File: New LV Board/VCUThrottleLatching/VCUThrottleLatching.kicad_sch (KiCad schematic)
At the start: 9 parts, among them J1 B12B-PH-K-S:JST_B12B-PH-K-S, U1 IRLML2060TRPBF, U2 IRLML2060TRPBF

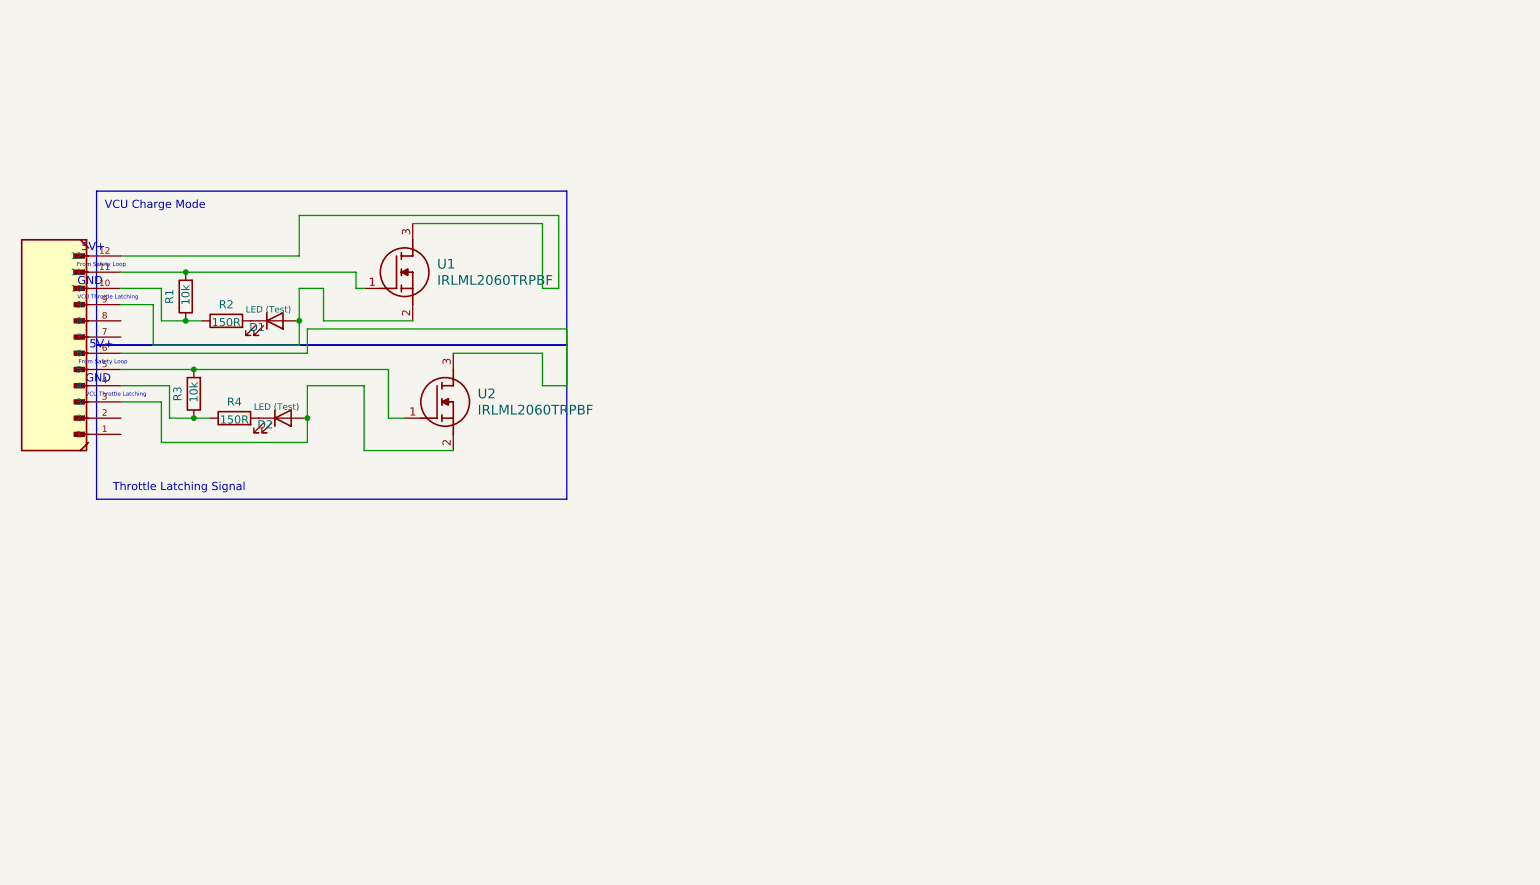
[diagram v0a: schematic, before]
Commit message: Precharge added to VCU Throttle Latching
Precharge Module
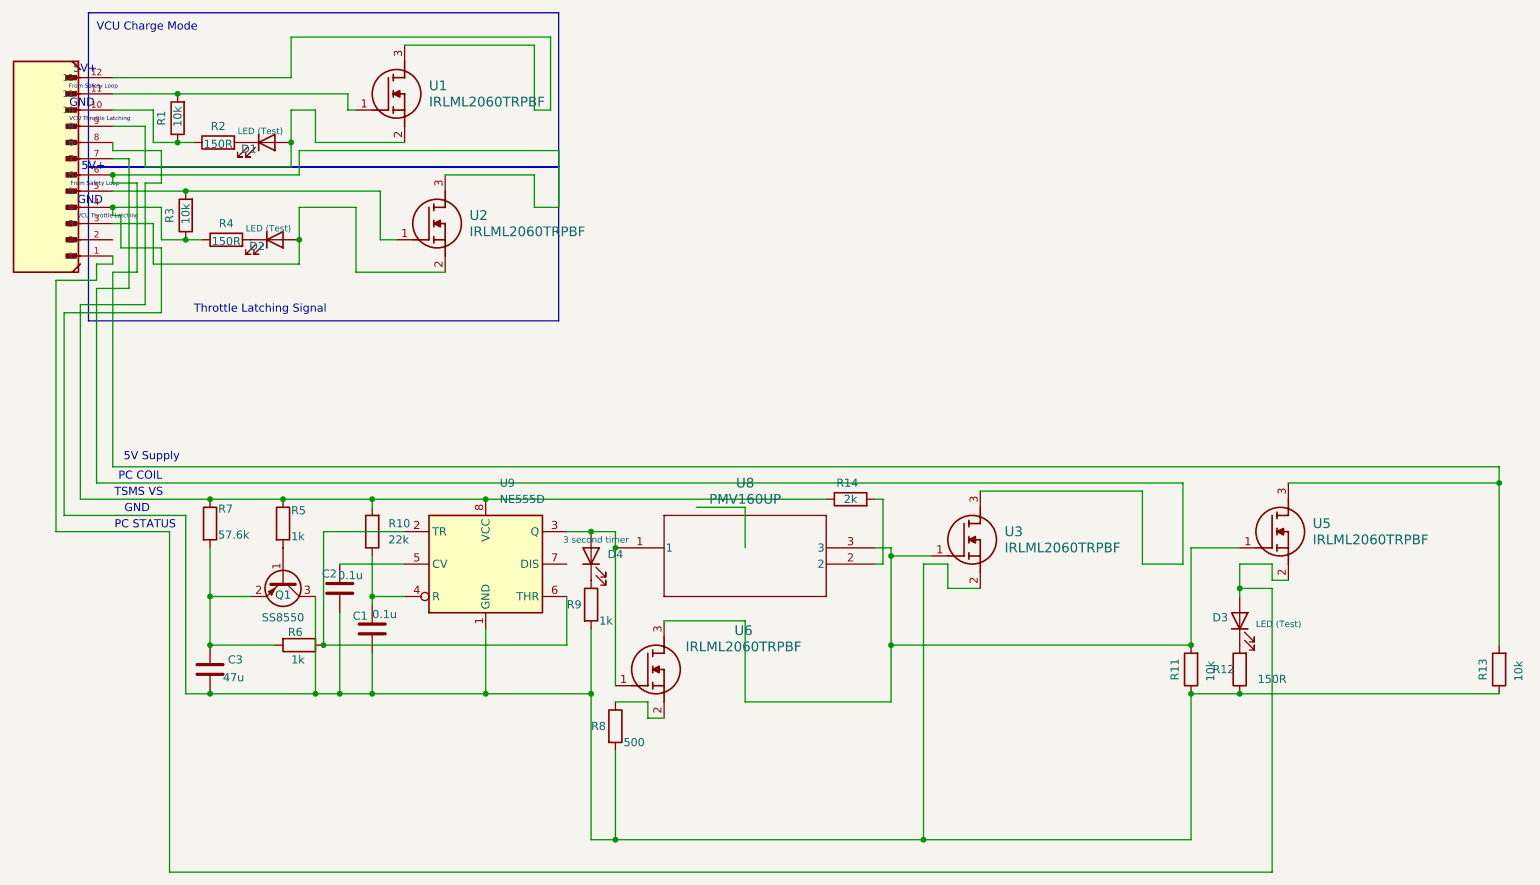
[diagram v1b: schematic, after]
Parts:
- added C1, C2: 0.1u, Capacitor_SMD:C_0201_0603Metric, symbol Device:C
- added C3: 47u, Capacitor_SMD:C_0201_0603Metric, symbol Device:C
- added D3: LED (Test), LED_THT:LED_D3.0mm, symbol Device:LED
- added D4: 3 second timer, LED_THT:LED_D3.0mm, symbol Device:LED
- added Q1: SS8550, Footprints:SOT95P237X112-3N, symbol Transistor_BJT:SS8550
- added R10: 22k, Footprints:STA_CF14_STP, symbol Device:R
- added R11, R13: 10k, Footprints:STA_CF14_STP, symbol Device:R
- added R12: 150R, Footprints:STA_CF14_STP, symbol Device:R
- added R14: 2k, Footprints:STA_CF14_STP, symbol Device:R
- added R5, R6, R9: 1k, Footprints:STA_CF14_STP, symbol Device:R
- added R7: 57.6k, Footprints:STA_CF14_STP, symbol Device:R
- added R8: 500, Footprints:STA_CF14_STP, symbol Device:R
- added U3, U5, U6: IRLML2060TRPBF, SOT95P237X112-3N, symbol IRLML2060TRPBF:IRLML2060TRPBF
- added U8: PMV160UP, Footprints:SOIC127P599X175-8N, symbol 2025-09-16_20-26-56:PMV160UP
- added U9: NE555D, Footprints:SOIC127P599X175-8N, symbol Timer:NE555D
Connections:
- net at J1.4, R3.1, R4.1: now also C1.2, C2.2, C3.2, Q1.3 (C), R11.1, R12.1, R13.1, R8.2, R9.2, U3.2 (S), U9.1 (GND)
- net at J1.1: now also D3.2 (A), U5.2 (S)
- net at J1.6, U2.3 (D): now also R13.2, U5.3 (D)
- net at J1.7: now also U3.3 (D)
- net at J1.8: now also R10.2, R14.1, R5.1, R7.1, U9.8 (VCC)
- new net: D3.1 (K), R12.2
- new net: D4.2 (A), U6.1 (G), U8.1, U9.3 (Q)
- new net: R8.1, U6.2 (S)
- new net: R11.2, U3.1 (G), U5.1 (G), U6.3 (D), U8.3
- new net: Q1.1 (B), R5.2
- new net: C3.1, Q1.2 (E), R6.2, R7.2
- new net: R6.1, U9.2 (TR), U9.6 (THR)
- new net: C1.1, R10.1, U9.4 (R)
- new net: C2.1, U9.5 (CV)
- new net: R14.2, U8.2
- new net: D4.1 (K), R9.1
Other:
- note added: "5V Supply"
- note added: "PC COIL"
- note added: "PC STATUS"
- note added: "TSMS VS"
- moved on the sheet: D1, D2, R1, R2, R3, R4, U1, U2
